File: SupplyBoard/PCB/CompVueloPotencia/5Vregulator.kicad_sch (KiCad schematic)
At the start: 0 parts

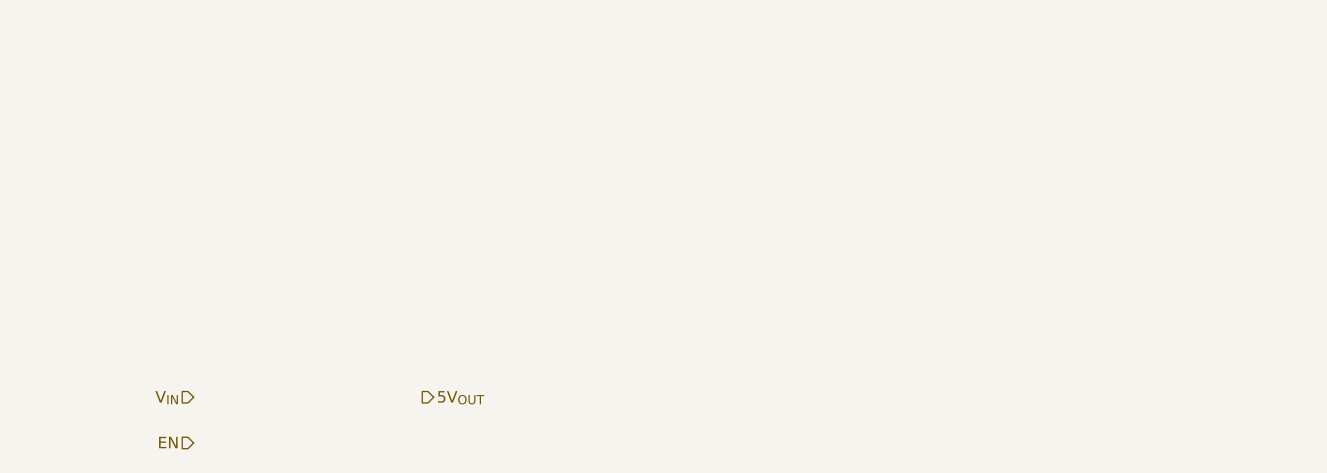
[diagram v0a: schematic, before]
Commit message: SupplyBoard - finish current sense
Finish the Current Sensor Circuit and add more 3.3V out, i change de microcontroles to a mcu that have the exact GPIO's
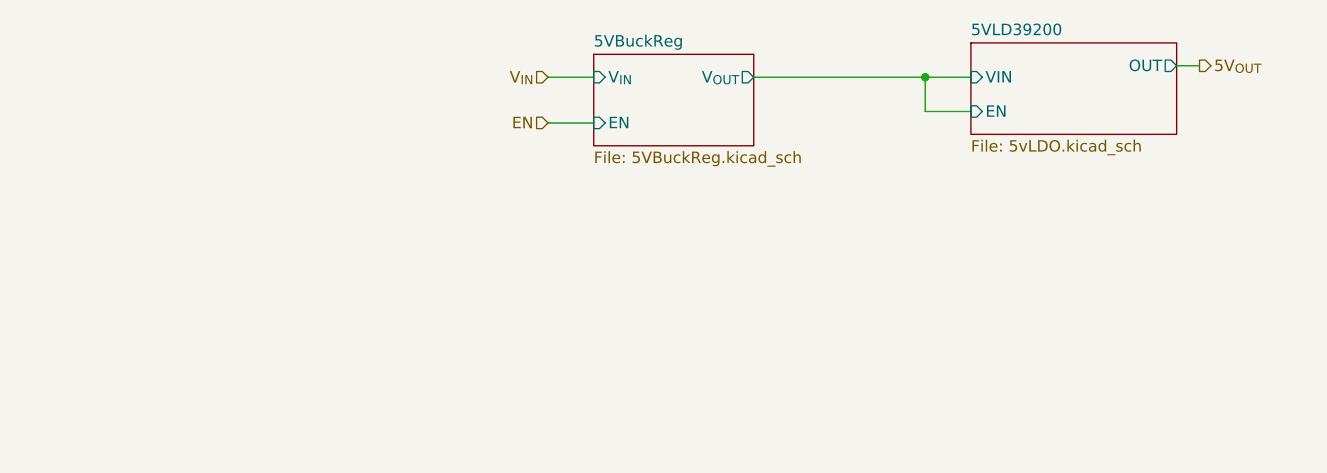
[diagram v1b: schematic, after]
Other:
- added sheet 5VBuckReg (5VBuckReg.kicad_sch)
- added sheet 5VLD39200 (5vLDO.kicad_sch)
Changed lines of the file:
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@@
 	(generator_version "9.0")
 	(paper "A4")
+	(junction
+		(at 140.97 34.29)
+		(diameter 0)
+		(color 0 0 0 0)
+	)
+	(wire
+		(pts
+			(xy 140.97 38.1) (xy 146.05 38.1)
+		)
+		(stroke
+			(width 0)
+			(type default)
+		)
+	)
+	(wire
+		(pts
+			(xy 171.45 33.02) (xy 168.91 33.02)
+		)
+		(stroke
+			(width 0)
+			(type default)
+		)
+	)
+	(wire
+		(pts
+			(xy 140.97 34.29) (xy 140.97 38.1)
+		)
+		(stroke
+			(width 0)
+			(type default)
+		)
+	)
+	(wire
+		(pts
+			(xy 99.06 34.29) (xy 104.14 34.29)
+		)
+		(stroke
+			(width 0)
+			(type default)
+		)
+	)
+	(wire
+		(pts
+			(xy 121.92 34.29) (xy 140.97 34.29)
+		)
+		(stroke
+			(width 0)
+			(type default)
+		)
+	)
+	(wire
+		(pts
+			(xy 99.06 39.37) (xy 104.14 39.37)
+		)
+		(stroke
+			(width 0)
+			(type default)
+		)
+	)
+	(wire
+		(pts
+			(xy 140.97 34.29) (xy 146.05 34.29)
+		)
+		(stroke
+			(width 0)
+			(type default)
+		)
+	)
 	(hierarchical_label "EN"
 		(shape input)
-		(at 59.69 74.93 180)
+		(at 99.06 39.37 180)
 		(effects
 			(font
@@
 	(hierarchical_label "5V_{OUT}"
 		(shape output)
-		(at 85.09 69.85 0)
+		(at 171.45 33.02 0)
 		(effects
 			(font
@@
 	(hierarchical_label "V_{IN}"
 		(shape input)
-		(at 59.69 69.85 180)
+		(at 99.06 34.29 180)
 		(effects
 			(font
@@
 		)
 	)
+	(sheet
+		(at 104.14 31.75)
+		(size 17.78 10.16)
+		(exclude_from_sim no)
+		(in_bom yes)
+		(on_board yes)
+		(dnp no)
+		(fields_autoplaced yes)
+		(stroke
+			(width 0.1524)
+			(type solid)
+		)
+		(fill
+			(color 0 0 0 0.0000)
+		)
+		(property "Sheetname" "5VBuckReg"
+			(at 104.14 31.0384 0)
+			(effects
+				(font
+					(size 1.27 1.27)
+				)
+				(justify left bottom)
+			)
+		)
+		(property "Sheetfile" "5VBuckReg.kicad_sch"
+			(at 104.14 42.4946 0)
+			(effects
+				(font
+					(size 1.27 1.27)
+				)
+				(justify left top)
+			)
+		)
+		(pin "EN" input
+			(at 104.14 39.37 180)
+			(effects
+				(font
+					(size 1.27 1.27)
+				)
+				(justify left)
+			)
+		)
+		(pin "V_{IN}" input
+			(at 104.14 34.29 180)
+			(effects
+				(font
+					(size 1.27 1.27)
+				)
+				(justify left)
+			)
+		)
+		(pin "V_{OUT}" output
+			(at 121.92 34.29 0)
+			(effects
+				(font
+					(size 1.27 1.27)
+				)
+				(justify right)
+			)
+		)
+		(instances
+			(project "SupplyBoardCompVuelo"
+				(path "/2119c5ce-afa8-4b00-8fd4-fc653d4beb45/22ae39d6-ba46-47bf-81b8-3d66f18a6610/efcc7e4b-243b-4527-8c15-6d23e19f631a"
+					(page "15")
+				)
+			)
+		)
+	)
+	(sheet
+		(at 146.05 30.48)
+		(size 22.86 10.16)
+		(exclude_from_sim no)
+		(in_bom yes)
+		(on_board yes)
+		(dnp no)
+		(fields_autoplaced yes)
+		(stroke
+			(width 0.1524)
+			(type solid)
+		)
+		(fill
+			(color 0 0 0 0.0000)
+		)
+		(property "Sheetname" "5VLD39200"
+			(at 146.05 29.7684 0)
+			(effects
+				(font
+					(size 1.27 1.27)
+				)
+				(justify left bottom)
+			)
+		)
+		(property "Sheetfile" "5vLDO.kicad_sch"
+			(at 146.05 41.2246 0)
+			(effects
+				(font
+					(size 1.27 1.27)
+				)
+				(justify left top)
+			)
+		)
+		(pin "EN" input
+			(at 146.05 38.1 180)
+			(effects
+				(font
+					(size 1.27 1.27)
+				)
+				(justify left)
+			)
+		)
+		(pin "OUT" output
+			(at 168.91 33.02 0)
+			(effects
+				(font
+					(size 1.27 1.27)
+				)
+				(justify right)
+			)
+		)
+		(pin "VIN" input
+			(at 146.05 34.29 180)
+			(effects
+				(font
+					(size 1.27 1.27)
+				)
+				(justify left)
+			)
+		)
+		(instances
+			(project "SupplyBoardCompVuelo"
+				(path "/2119c5ce-afa8-4b00-8fd4-fc653d4beb45/22ae39d6-ba46-47bf-81b8-3d66f18a6610/efcc7e4b-243b-4527-8c15-6d23e19f631a"
+					(page "16")
+				)
+			)
+		)
+	)

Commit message: SupplyBoard - update layout
schematic completed and PCB layout started; only the routing of the traces remains to be done
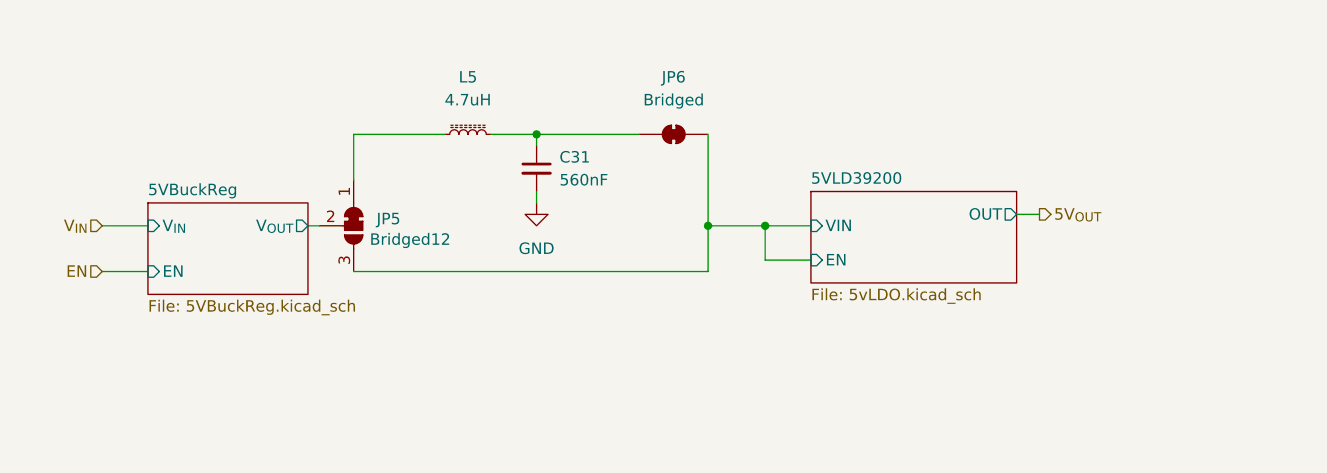
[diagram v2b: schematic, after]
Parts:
- added C31: 560nF, Capacitor_SMD:C_0805_2012Metric_Pad1.18x1.45mm_HandSolder, symbol Device:C_Small
- added JP5: Bridged12, Jumper:SolderJumper-3_P1.3mm_Bridged12_RoundedPad1.0x1.5mm, symbol Jumper:SolderJumper_3_Bridged12
- added JP6: Bridged, Jumper:SolderJumper-2_P1.3mm_Bridged_RoundedPad1.0x1.5mm, symbol Jumper:SolderJumper_2_Bridged
- added L5: 4.7uH, Inductor_SMD:L_Bourns_SRN6045TA, symbol Device:L_Ferrite_Small
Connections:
- net 5VBuckReg/V_{OUT}: now also JP5.2 (C)
- new net: C31.1, JP6.1 (A), L5.2
- new net: JP5.1 (A), L5.1
- new net 5VLD39200/EN: JP5.3 (B), JP6.2 (B)
- new net GND: C31.2
